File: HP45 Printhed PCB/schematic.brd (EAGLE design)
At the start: 35.6 x 59.9 mm, 42 parts, among them P1 0930, P2 0930, P3 0930, P4 0930

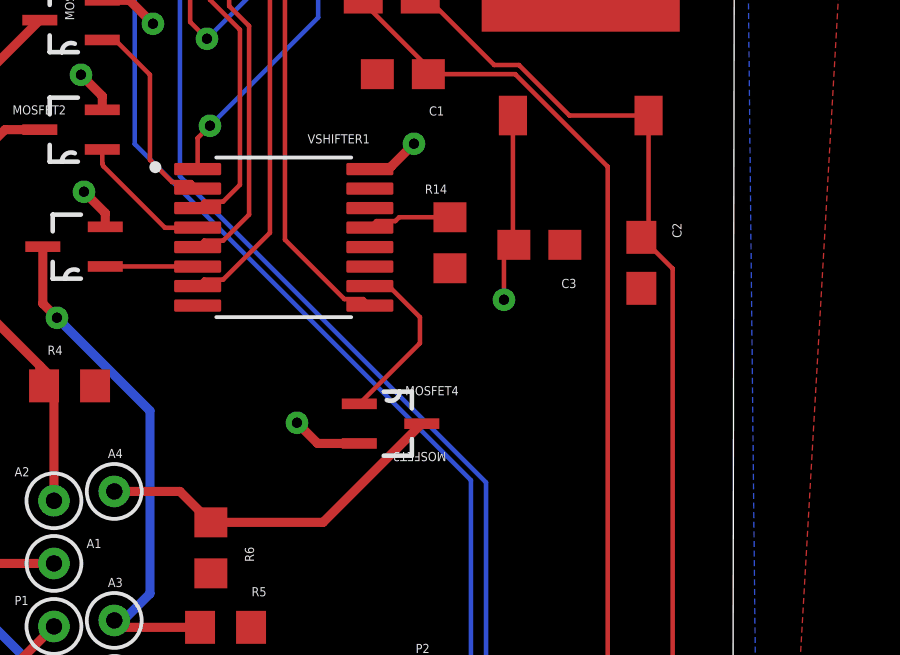
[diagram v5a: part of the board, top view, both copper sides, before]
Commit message: Smaller Fixes
Follow up for adding resistors
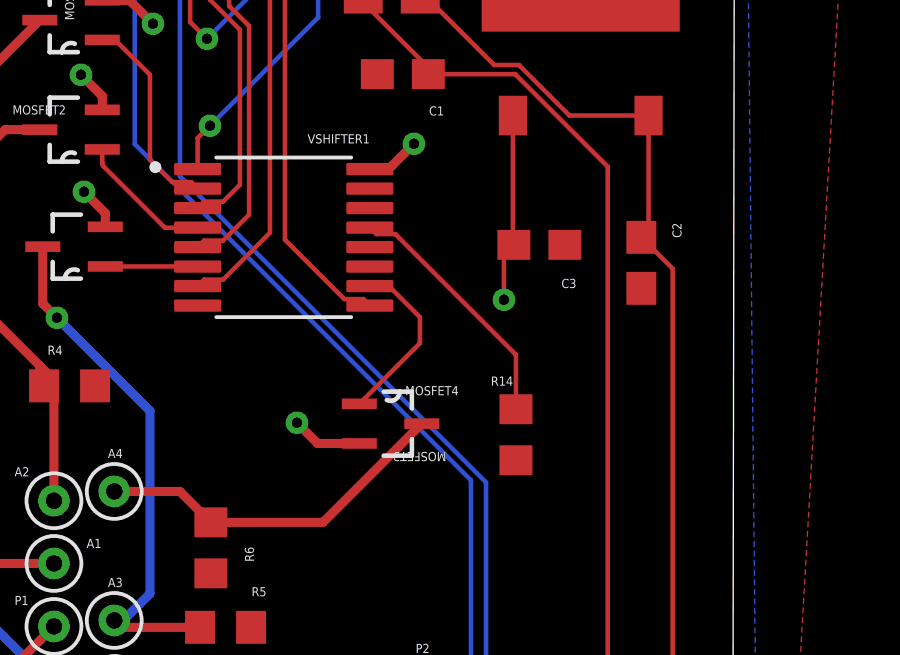
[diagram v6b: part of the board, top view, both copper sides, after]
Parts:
- moved R14 6.77 mm to (27.7, 32.2)
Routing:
- net N$13: track 2.81 -> 8.44 mm
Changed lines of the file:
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@@
 <attribute name="VALUE" x="8.535" y="47.405" size="1.27" layer="27" rot="R180"/>
 </element>
-<element name="R14" library="rcl" library_urn="urn:adsk.eagle:library:334" package="R0603" package3d_urn="urn:adsk.eagle:package:23555/2" value="10Ω" x="25.5" y="38.6" smashed="yes" rot="R90">
-<attribute name="NAME" x="24.665" y="40.235" size="0.3048" layer="25"/>
-<attribute name="SPICEPREFIX" value="R" x="25.5" y="38.6" size="1.778" layer="27" rot="R90" display="off"/>
-<attribute name="VALUE" x="27.405" y="37.965" size="1.27" layer="27" rot="R90"/>
+<element name="R14" library="rcl" library_urn="urn:adsk.eagle:library:334" package="R0603" package3d_urn="urn:adsk.eagle:package:23555/2" value="10Ω" x="27.7" y="32.2" smashed="yes" rot="R90">
+<attribute name="NAME" x="26.865" y="33.835" size="0.3048" layer="25"/>
+<attribute name="SPICEPREFIX" value="R" x="27.7" y="32.2" size="1.778" layer="27" rot="R90" display="off"/>
+<attribute name="VALUE" x="29.605" y="31.565" size="1.27" layer="27" rot="R90"/>
 </element>
 </elements>
@@
 <contactref element="R14" pad="2"/>
 <contactref element="VSHIFTER1" pad="13"/>
-<wire x1="25.5" y1="39.45" x2="23.80826875" y2="39.45" width="0.1524" layer="1"/>
-<wire x1="23.80826875" y1="39.45" x2="23.67966875" y2="39.3214" width="0.1524" layer="1"/>
-<wire x1="23.67966875" y1="39.3214" x2="23.0464" y2="39.3214" width="0.1524" layer="1"/>
-<wire x1="23.0464" y1="39.3214" x2="22.83" y2="39.105" width="0.1524" layer="1"/>
+<wire x1="22.83" y1="39.105" x2="23.0464" y2="38.8886" width="0.1524" layer="1"/>
+<wire x1="23.0464" y1="38.8886" x2="23.67966875" y2="38.8886" width="0.1524" layer="1"/>
+<wire x1="23.67966875" y1="38.8886" x2="27.7" y2="34.86826875" width="0.1524" layer="1"/>
+<wire x1="27.7" y1="34.86826875" x2="27.7" y2="33.05" width="0.1524" layer="1"/>
 </signal>
 <signal name="N$14">
